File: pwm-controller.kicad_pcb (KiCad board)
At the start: 4 copper layers, 50 x 50 mm, 55 parts, among them J1 DEBUG_ADDRESS_I2C_INT, J2 POWER, J3 OUT+, J4 OUT-, Q1 MMBT5551, Q2 SiS402DN, Q3 MMBT5401, Q4 MMBT5551, Q5 SiS402DN, Q6 MMBT5401, Q7 MMBT5551, Q8 MMBT5551, SW1 EC12D1524403, U1 STM8S003F3Px, U2 78L05

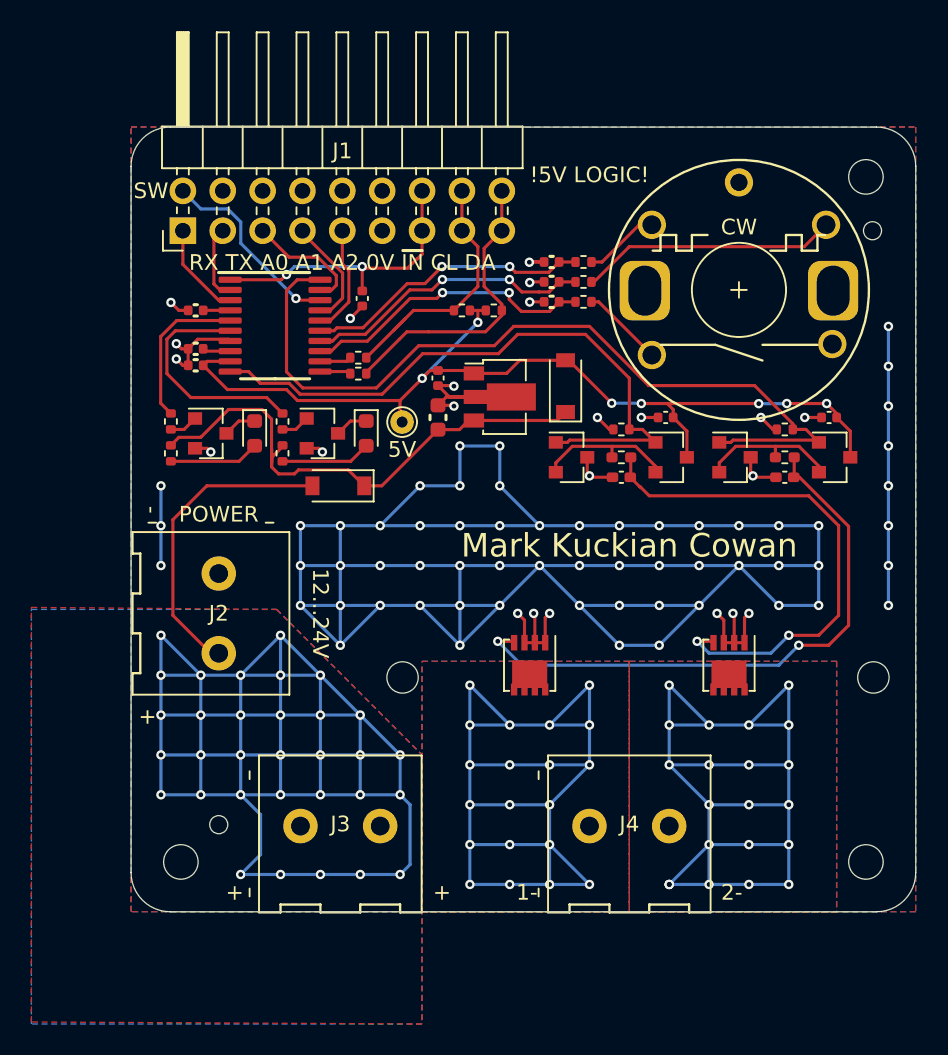
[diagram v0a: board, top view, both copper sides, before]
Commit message: add mosfets, fix led+i2c resistors
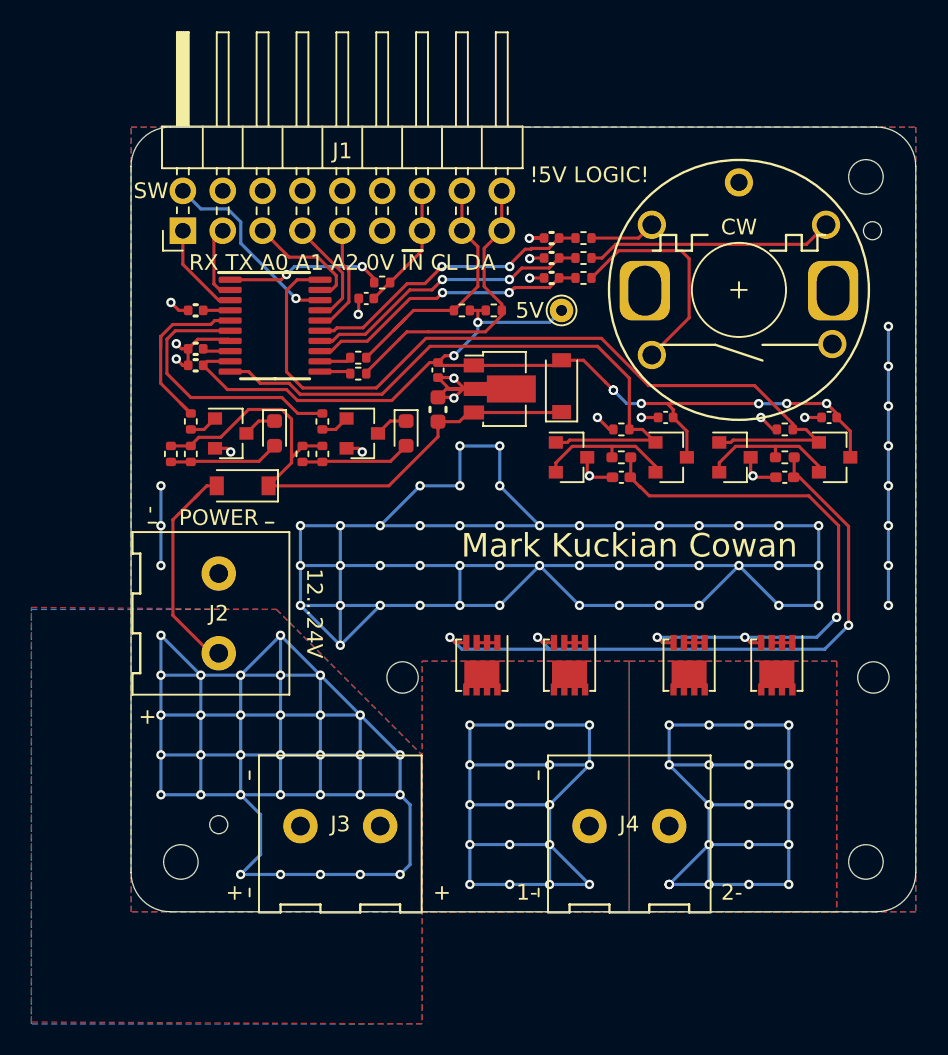
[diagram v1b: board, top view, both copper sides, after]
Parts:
- removed the R13 at (78.7, 97.0)
- added Q3: SiS402DN, Package_SO:Vishay_PowerPAK_1212-8_Single, F.Cu at (117.3, 110.5)
- added Q7: SiS402DN, Package_SO:Vishay_PowerPAK_1212-8_Single, F.Cu at (104.1, 110.5)
- added R14: 4.7k, Resistor_SMD:R_0402_1005Metric, F.Cu at (78.7, 97.0)
- added R17: 4.7k, Resistor_SMD:R_0402_1005Metric, F.Cu at (87.1, 97.0)
- added R18: 4.7k, Resistor_SMD:R_0402_1005Metric, F.Cu at (88.4, 97.0)
- added R4: 100, Resistor_SMD:R_0402_1005Metric, F.Cu at (92.2, 86.1)
- R1, R2: value 220 -> 100
- R11: renamed from R10; value 220 -> 100
- R15: value 220 -> 4.7k
- R6: renamed from R5; value 220 -> 100
- R7: renamed from R6; value 220 -> 100
- R8: renamed from R7; value 220 -> 100
- R9: renamed from R8; value 220 -> 100
- moved TP1 12.4 mm to (103.6, 87.9)
- moved D2 6.10 mm to (83.3, 99.1)
- moved R15 5.84 mm to (80.0, 97.0), turned to 270 degrees
- moved Q6 3.05 mm to (98.6, 110.5)
- moved Q10 2.54 mm to (90.9, 95.7)
- moved D4 2.54 mm to (93.7, 95.7)
- moved Q2 2.54 mm to (111.8, 110.5)
- moved R16 2.54 mm to (88.4, 95.0)
- moved C7 1.52 mm to (103.0, 83.3)
- moved C8 1.52 mm to (103.0, 84.5)
- moved C9 1.52 mm to (103.0, 85.8)
- moved R6 1.52 mm to (105.0, 83.3)
- moved R7 1.52 mm to (105.0, 85.8)
- moved R8 1.52 mm to (105.0, 84.5)
- moved R13 1.27 mm to (80.0, 95.0)
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- renumbered Q8 to Q10, Q3 to Q4, Q4 to Q5, Q5 to Q6, Q6 to Q8, Q7 to Q9, R9 to R10, R11 to R12, R12 to R13, R14 to R16, R4 to R5
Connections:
- R15 pad 1: /led_driver2/LED_A -> VIN_D
- R15 pad 2: VIN_D -> /led_driver1/LED_A
- U1 pad 1: INT -> /INT_PIN
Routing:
- net GND: track 237.1 -> 211.6 mm, vias 83 -> 74
- net DRAIN1: track 70.2 -> 58.0 mm, vias 21 -> 19
- net DRAIN2: track 70.2 -> 58.0 mm, vias 20 -> 18
- net INT: track 18.6 -> 8.15 mm, vias 2 -> 0
- net /INT_PIN: track 0.00 -> 10.1 mm, vias 0 -> 2
- net Net-(R7-Pad2): track 5.25 -> 14.3 mm
- net VIN: track 163.8 -> 158.1 mm
- net /channel2/GATE: track 37.5 -> 42.2 mm, vias 2 -> 3
- net +5V: track 61.2 -> 64.4 mm, vias 7 -> 8
- net /channel1/GATE: track 33.0 -> 36.1 mm, vias 2 -> 3
- net LED2: track 14.9 -> 17.4 mm
- net VIN_D: track 35.1 -> 37.6 mm
- net LED1: track 10.0 -> 12.2 mm
- net /led_driver2/LED_A: track 5.75 -> 7.02 mm
- net /led_driver1/LED_A: track 5.75 -> 7.02 mm
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
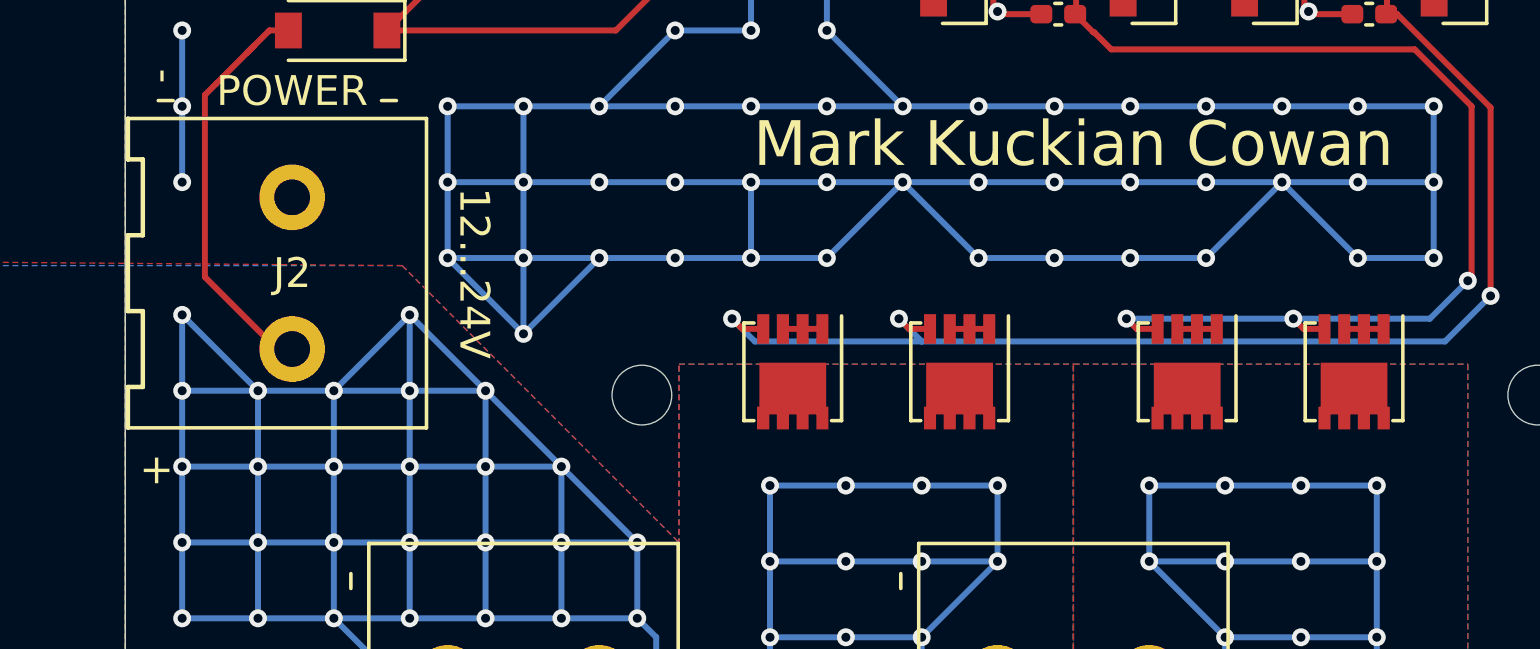
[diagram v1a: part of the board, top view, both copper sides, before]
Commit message: going to swap LEDs and 5V supply over in layout
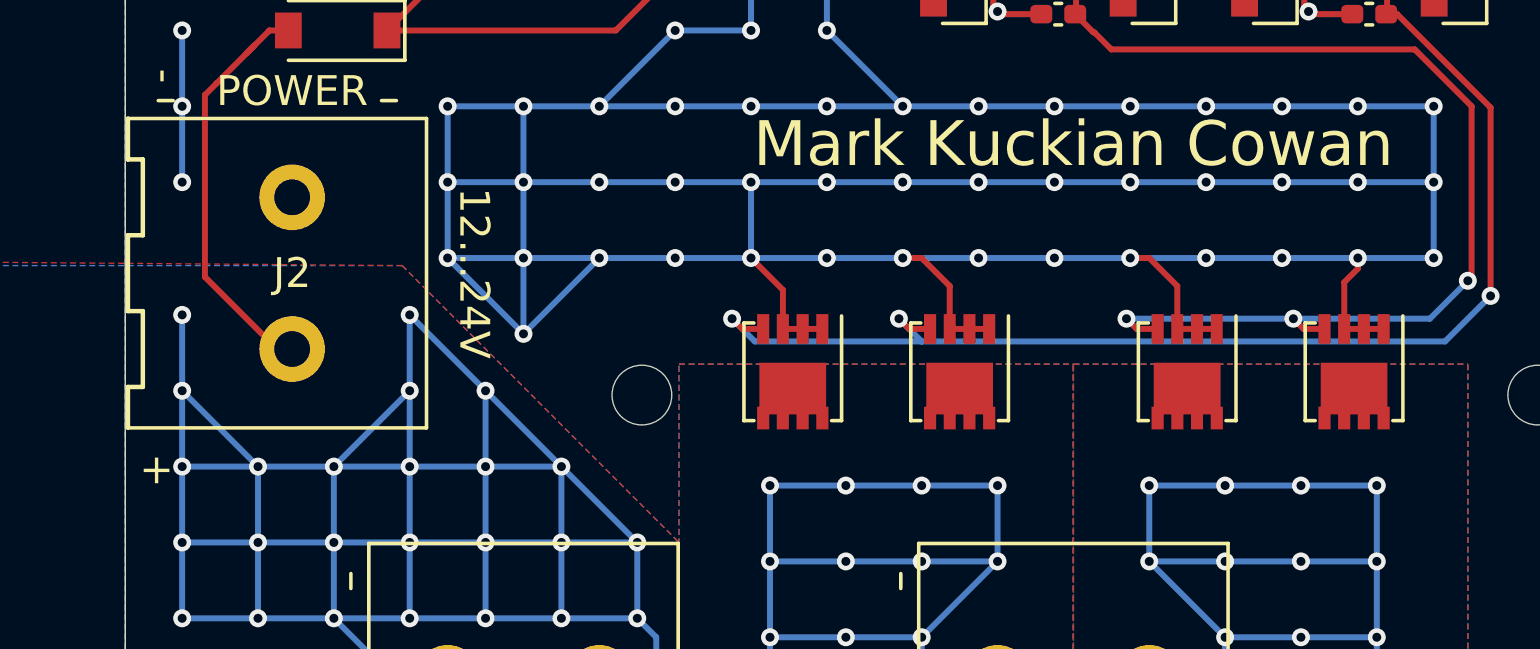
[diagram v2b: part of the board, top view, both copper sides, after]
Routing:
- net VIN: track 158.1 -> 142.8 mm, vias 32 -> 30
- net GND: track 211.6 -> 219.5 mm, vias 74 -> 76
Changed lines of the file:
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@@
     (thickness 1.6)
     (drawings 22)
-    (tracks 699)
+    (tracks 705)
     (zones 0)
     (modules 60)
@@
     (last_trace_width 0.2)
     (trace_clearance 0.2)
-    (zone_clearance 0.635)
-    (zone_45_only yes)
+    (zone_clearance 0.5)
+    (zone_45_only no)
     (trace_min 0.2)
     (via_size 0.6)
@@
   (via (at 107.315 106.68) (size 0.6) (drill 0.3) (layers F.Cu B.Cu) (net 1))
   (segment (start 109.855 106.68) (end 107.315 106.68) (width 0.2) (layer B.Cu) (net 1))
-  (segment (start 112.395 106.68) (end 114.935 104.14) (width 0.2) (layer B.Cu) (net 1))
   (segment (start 97.155 106.68) (end 99.695 106.68) (width 0.2) (layer B.Cu) (net 1))
-  (segment (start 99.695 106.68) (end 102.235 104.14) (width 0.2) (layer B.Cu) (net 1))
   (via (at 124.46 106.68) (size 0.6) (drill 0.3) (layers F.Cu B.Cu) (net 1))
   (segment (start 124.46 104.14) (end 124.46 106.68) (width 0.2) (layer B.Cu) (net 1))
@@
   (via (at 104.775 106.68) (size 0.6) (drill 0.3) (layers F.Cu B.Cu) (net 1))
   (segment (start 107.315 106.68) (end 104.775 106.68) (width 0.2) (layer B.Cu) (net 1))
-  (segment (start 104.775 106.68) (end 102.235 104.14) (width 0.2) (layer B.Cu) (net 1))
   (via (at 117.475 106.68) (size 0.6) (drill 0.3) (layers F.Cu B.Cu) (net 1))
   (segment (start 120.015 106.68) (end 117.475 106.68) (width 0.2) (layer B.Cu) (net 1))
-  (segment (start 117.475 106.68) (end 114.935 104.14) (width 0.2) (layer B.Cu) (net 1))
   (via (at 78.105 99.06) (size 0.6) (drill 0.3) (layers F.Cu B.Cu) (net 1))
   (via (at 78.105 101.6) (size 0.6) (drill 0.3) (layers F.Cu B.Cu) (net 1))
@@
   (segment (start 117.018 109.055) (end 118.338 109.055) (width 0.2) (layer F.Cu) (net 1))
   (segment (start 103.81 109.055) (end 105.13 109.055) (width 0.2) (layer F.Cu) (net 1))
+  (via (at 114.935 106.68) (size 0.6) (drill 0.3) (layers F.Cu B.Cu) (net 1))
+  (segment (start 117.475 106.68) (end 114.935 106.68) (width 0.2) (layer B.Cu) (net 1))
+  (segment (start 114.935 106.68) (end 112.395 106.68) (width 0.2) (layer B.Cu) (net 1))
+  (via (at 102.235 106.68) (size 0.6) (drill 0.3) (layers F.Cu B.Cu) (net 1))
+  (segment (start 104.775 106.68) (end 102.235 106.68) (width 0.2) (layer B.Cu) (net 1))
+  (segment (start 102.235 106.68) (end 99.695 106.68) (width 0.2) (layer B.Cu) (net 1))
+  (segment (start 98.222 107.747) (end 97.155 106.68) (width 0.2) (layer F.Cu) (net 1))
+  (segment (start 98.222 109.055) (end 98.222 107.747) (width 0.2) (layer F.Cu) (net 1))
+  (segment (start 103.81 109.055) (end 103.81 107.62) (width 0.2) (layer F.Cu) (net 1))
+  (segment (start 102.87 106.68) (end 102.235 106.68) (width 0.2) (layer F.Cu) (net 1))
+  (segment (start 103.81 107.62) (end 102.87 106.68) (width 0.2) (layer F.Cu) (net 1))
+  (segment (start 111.43 109.055) (end 111.43 107.62) (width 0.2) (layer F.Cu) (net 1))
+  (segment (start 111.43 107.62) (end 110.49 106.68) (width 0.2) (layer F.Cu) (net 1))
+  (segment (start 110.49 106.68) (end 109.855 106.68) (width 0.2) (layer F.Cu) (net 1))
+  (segment (start 117.018 109.055) (end 117.018 107.493) (width 0.2) (layer F.Cu) (net 1))
+  (segment (start 117.018 107.493) (end 117.475 107.036) (width 0.2) (layer F.Cu) (net 1))
+  (segment (start 117.475 107.036) (end 117.475 106.68) (width 0.2) (layer F.Cu) (net 1))
   (segment (start 80.799 87.879) (end 80.798 87.88) (width 0.2) (layer F.Cu) (net 2) (status 30))
   (segment (start 82.5165 87.879) (end 80.799 87.879) (width 0.2) (layer F.Cu) (net 2) (status 30))
@@
   (via (at 85.725 111.125) (size 0.6) (drill 0.3) (layers F.Cu B.Cu) (net 23))
   (segment (start 85.725 113.665) (end 85.725 111.125) (width 0.2) (layer B.Cu) (net 23))
-  (via (at 83.185 111.125) (size 0.6) (drill 0.3) (layers F.Cu B.Cu) (net 23))
-  (segment (start 83.185 113.665) (end 83.185 111.125) (width 0.2) (layer B.Cu) (net 23))
-  (segment (start 83.185 111.125) (end 88.265 111.125) (width 0.2) (layer B.Cu) (net 23))
-  (via (at 80.645 111.125) (size 0.6) (drill 0.3) (layers F.Cu B.Cu) (net 23))
-  (segment (start 80.645 113.665) (end 80.645 111.125) (width 0.2) (layer B.Cu) (net 23))
-  (segment (start 83.185 111.125) (end 80.645 111.125) (width 0.2) (layer B.Cu) (net 23))
-  (segment (start 80.645 111.125) (end 78.105 111.125) (width 0.2) (layer B.Cu) (net 23))
-  (segment (start 80.645 111.125) (end 78.105 108.585) (width 0.2) (layer B.Cu) (net 23))
   (via (at 85.725 108.585) (size 0.6) (drill 0.3) (layers F.Cu B.Cu) (net 23))
   (segment (start 85.725 111.125) (end 85.725 108.585) (width 0.2) (layer B.Cu) (net 23))
   (segment (start 88.265 111.125) (end 85.725 108.585) (width 0.2) (layer B.Cu) (net 23))
-  (segment (start 85.725 108.585) (end 83.185 111.125) (width 0.2) (layer B.Cu) (net 23))
   (via (at 83.185 123.825) (size 0.6) (drill 0.3) (layers F.Cu B.Cu) (net 23))
   (via (at 85.725 123.825) (size 0.6) (drill 0.3) (layers F.Cu B.Cu) (net 23))
@@
   (segment (start 80.264 99.822) (end 79.248 100.838) (width 0.2) (layer F.Cu) (net 23))
   (segment (start 80.518 99.568) (end 80.264 99.822) (width 0.2) (layer F.Cu) (net 23))
+  (segment (start 78.105 111.125) (end 80.645 113.665) (width 0.2) (layer B.Cu) (net 23))
+  (segment (start 85.725 111.125) (end 83.185 113.665) (width 0.2) (layer B.Cu) (net 23))
   (segment (start 81.049 91.129) (end 80.798 91.38) (width 0.2) (layer F.Cu) (net 24) (status 30))
   (segment (start 82.5165 91.129) (end 81.049 91.129) (width 0.2) (layer F.Cu) (net 24) (status 30))
@@
   )
   (zone (net 1) (net_name GND) (layer F.Cu) (hatch edge 0.508)
-    (connect_pads thru_hole_only (clearance 0.635))
+    (connect_pads thru_hole_only (clearance 0.5))
     (min_thickness 0.25)
     (fill yes (arc_segments 32) (thermal_gap 0.25) (thermal_bridge_width 0.5))

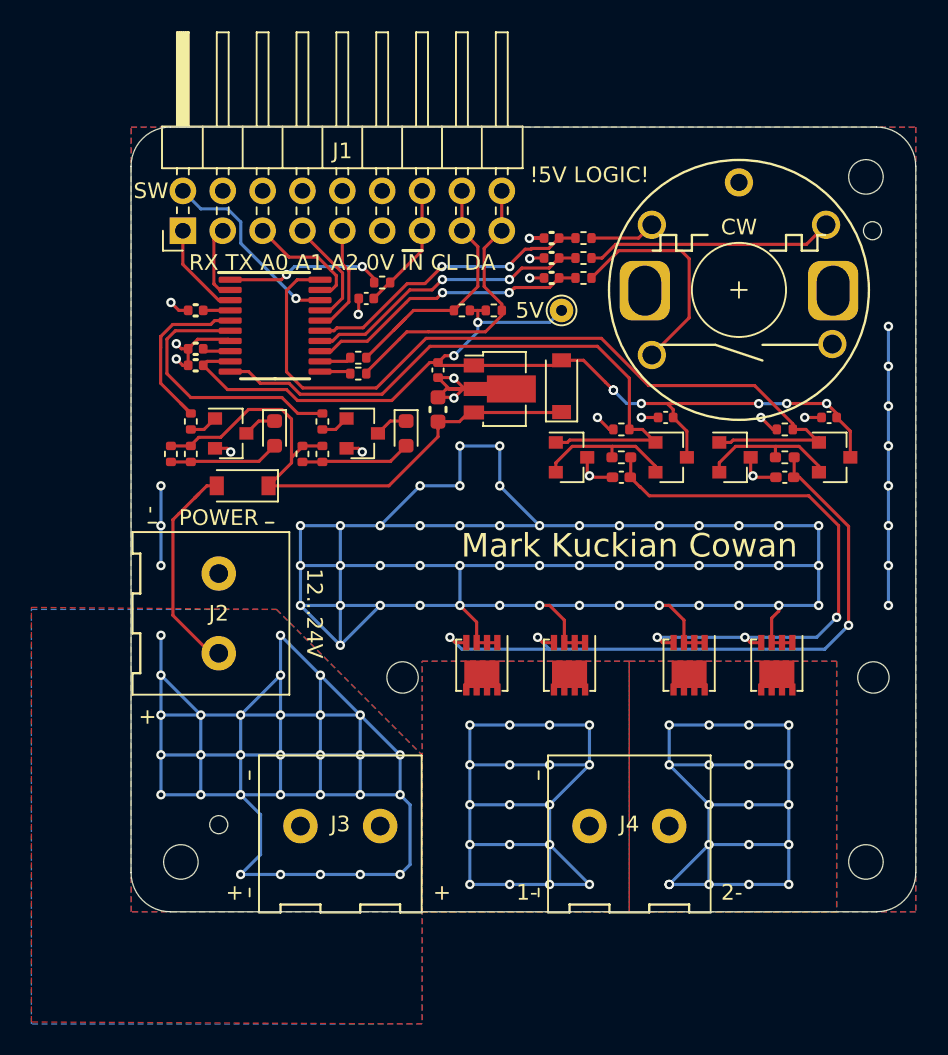
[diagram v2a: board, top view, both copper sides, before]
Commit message: swapped placement for 5V LDO vs LEDs, for more stable 5V supply when power-side of ground is noisy
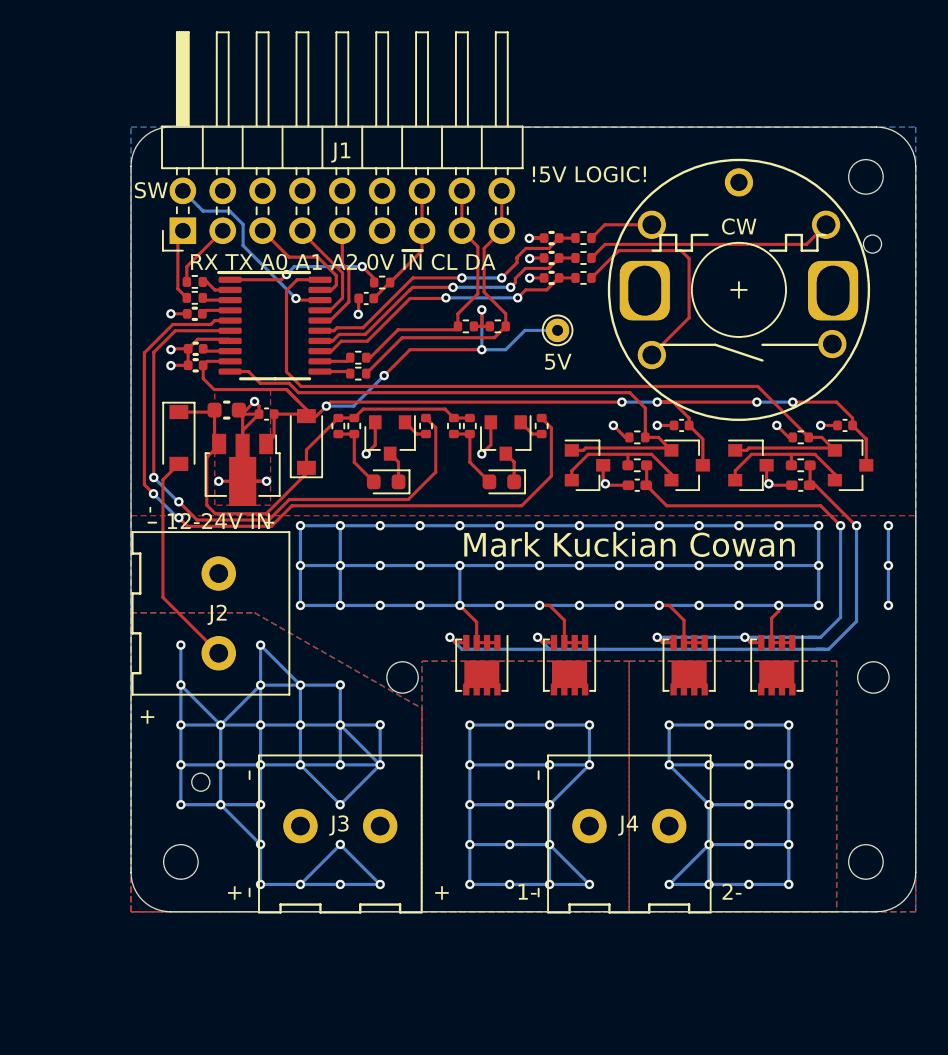
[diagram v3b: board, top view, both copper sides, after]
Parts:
- added R6: 100, Resistor_SMD:R_0402_1005Metric, F.Cu at (80.3, 86.1)
- added R7: 100, Resistor_SMD:R_0402_1005Metric, F.Cu at (80.3, 87.1)
- moved U2 17.2 mm to (83.3, 98.0), turned to 270 degrees
- moved D1 16.6 mm to (87.4, 96.3)
- moved R15 15.0 mm to (95.0, 95.2)
- moved R18 14.0 mm to (102.4, 95.2)
- moved C4 13.5 mm to (82.3, 94.2), turned to 0 degrees
- moved C5 11.3 mm to (84.8, 94.5), turned to 180 degrees
- moved R16 10.8 mm to (89.4, 95.2)
- moved R17 10.6 mm to (90.4, 95.2)
- moved Q9 10.2 mm to (92.7, 96.0), turned to 270 degrees
- moved R19 9.81 mm to (96.8, 95.2)
- moved R20 9.56 mm to (97.8, 95.2)
- moved Q10 9.15 mm to (100.1, 96.0), turned to 270 degrees
- moved D4 7.75 mm to (92.5, 98.8), turned to 180 degrees
- moved D3 6.83 mm to (99.8, 98.8), turned to 180 degrees
- moved D2 5.08 mm to (79.2, 96.0), turned to 270 degrees
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- renumbered D4 to D3, D3 to D4, R8 to R10, R9 to R11, R10 to R12, R11 to R13, R12 to R14, R13 to R15, R14 to R16, R15 to R17, R16 to R18, R17 to R19, R18 to R20, R6 to R8, R7 to R9
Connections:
- R15 pad 2: LED1 -> LED2
- R18 pad 2: LED2 -> LED1
- U1 pad 2: UTX -> /UTX_PIN
- U1 pad 3: URX -> /URX_PIN
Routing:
- net GND: track 219.5 -> 181.7 mm, vias 76 -> 63
- net LED1: track 12.2 -> 47.0 mm, vias 0 -> 2
- net LED2: track 17.4 -> 37.5 mm, vias 0 -> 2
- net +5V: track 64.4 -> 81.8 mm
- net VIN: track 142.8 -> 132.7 mm, vias 30 -> 28
- net VIN_D: track 37.6 -> 29.7 mm
- net /led_driver2/LED_A: track 7.02 -> 4.58 mm
- net /led_driver1/LED_A: track 7.02 -> 4.58 mm
- net PWM1: track 39.9 -> 37.8 mm
- net /URX_PIN: track 0.00 -> 2.07 mm
- net /UTX_PIN: track 0.00 -> 1.95 mm
- net PWM2: track 53.3 -> 51.4 mm
- net URX: track 6.37 -> 4.65 mm
- net SDA: track 19.1 -> 19.8 mm
- net UTX: track 4.82 -> 4.21 mm
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
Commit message: order ready
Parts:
- added G1: Roger, pwm-controller:roger, B.Cu at (100.1, 102.8)
- C10, C11, C12, C13, C2, C5, C6: value 100n/50 -> 100n
- C3, C7, C8, C9: value 3.3n -> 100n
- moved R4 0.76 mm to (91.4, 86.1)
- moved C3 0.26 mm to (91.4, 87.1), turned to 180 degrees
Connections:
- C3 pad 2: INT -> /INT_PIN
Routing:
- net +5V: track 81.8 -> 80.5 mm
- net INT: track 8.15 -> 6.96 mm
- net /INT_PIN: track 10.1 -> 11.1 mm
